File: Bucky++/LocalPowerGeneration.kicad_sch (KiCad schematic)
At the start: 26 parts, among them IC801 TPS629206QDRLRQ1, U2 TPS2116DRLR, U802 LMR36506MSC5RPERQ1

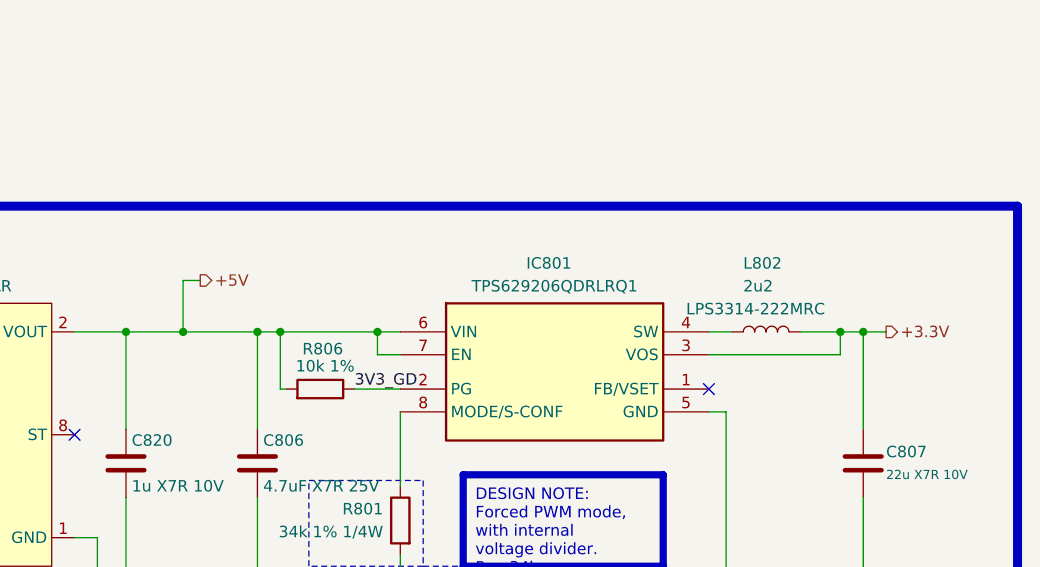
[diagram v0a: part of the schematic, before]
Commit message: added over-current protection on main input
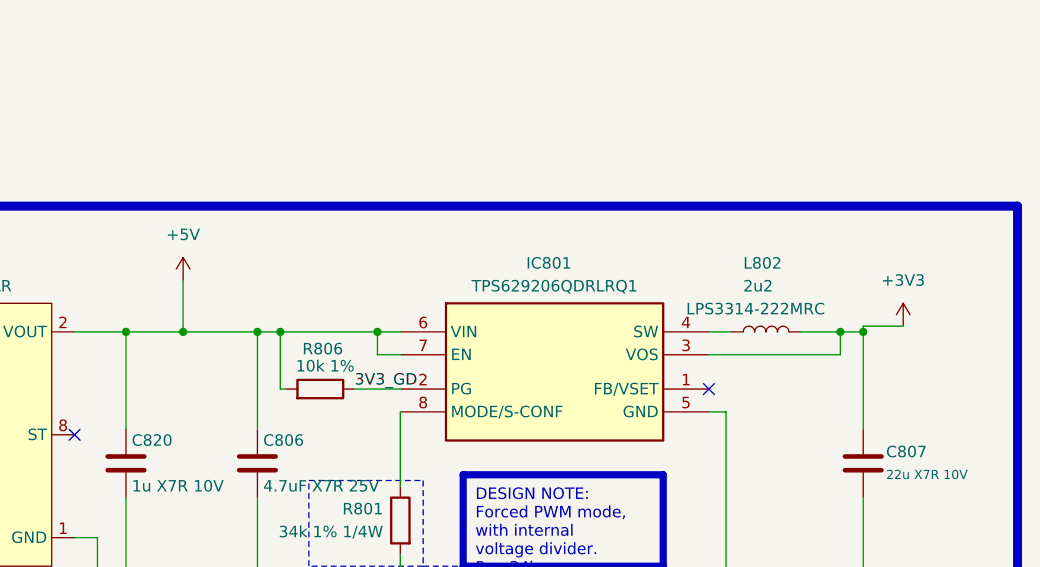
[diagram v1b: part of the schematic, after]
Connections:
- net +3.3V renamed +3V3
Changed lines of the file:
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@@
+	(wire
+		(pts
+			(xy 362.585 77.47) (xy 362.585 78.105)
+		)
+		(stroke
+			(width 0)
+			(type default)
+		)
+	)
 	(wire
 		(pts
@@
 	(wire
 		(pts
-			(xy 288.925 72.39) (xy 287.02 72.39)
-		)
-		(stroke
-			(width 0)
-			(type default)
-		)
-	)
-	(wire
-		(pts
 			(xy 174.625 78.105) (xy 172.085 78.105)
 		)
@@
 	(wire
 		(pts
-			(xy 362.585 78.105) (xy 365.125 78.105)
+			(xy 362.585 77.47) (xy 367.03 77.47)
 		)
 		(stroke
@@
 			)
 			(justify right)
-		)
-	)
-	(hierarchical_label "+3.3V"
-		(shape output)
-		(at 365.125 78.105 0)
-		(effects
-			(font
-				(size 1.27 1.27)
-			)
-			(justify left)
-		)
-	)
-	(hierarchical_label "+5V"
-		(shape output)
-		(at 288.925 72.39 0)
-		(effects
-			(font
-				(size 1.27 1.27)
-			)
-			(justify left)
 		)
 	)
@@
 	)
 	(symbol
+		(lib_id "power:+5V")
+		(at 287.02 72.39 0)
+		(unit 1)
+		(exclude_from_sim no)
+		(in_bom yes)
+		(on_board yes)
+		(dnp no)
+		(fields_autoplaced yes)
+		(property "Reference" "#PWR087"
+			(at 287.02 76.2 0)
+			(effects
+				(font
+					(size 1.27 1.27)
+				)
+				(hide yes)
+			)
+		)
+		(property "Value" "+5V"
+			(at 287.02 67.31 0)
+			(effects
+				(font
+					(size 1.27 1.27)
+				)
+			)
+		)
+		(property "Footprint" ""
+			(at 287.02 72.39 0)
+			(effects
+				(font
+					(size 1.27 1.27)
+				)
+				(hide yes)
+			)
+		)
+		(property "Datasheet" ""
+			(at 287.02 72.39 0)
+			(effects
+				(font
+					(size 1.27 1.27)
+				)
+				(hide yes)
+			)
+		)
+		(property "Description" "Power symbol creates a global label with name \"+5V\""
+			(at 287.02 72.39 0)
+			(effects
+				(font
+					(size 1.27 1.27)
+				)
+				(hide yes)
+			)
+		)
+		(pin "1"
+		)
+		(instances
+			(project ""
+				(path "/0650c7a8-acba-429c-9f8e-eec0baf0bc1c/fede4c36-00cc-4d3d-b71c-5243ba232202/20f2e49e-3c3c-4877-a054-2792c8a24538"
+					(reference "#PWR087")
+					(unit 1)
+				)
+			)
+		)
+	)
+	(symbol
 		(lib_id "Device:R")
 		(at 238.125 82.55 0)
@@
 					(unit 1)
 				)
+			)
+		)
+	)
+	(symbol
+		(lib_id "power:+3V3")
+		(at 367.03 77.47 0)
+		(unit 1)
+		(exclude_from_sim no)
+		(in_bom yes)
+		(on_board yes)
+		(dnp no)
+		(fields_autoplaced yes)
+		(property "Reference" "#PWR086"
+			(at 367.03 81.28 0)
+			(effects
+				(font
+					(size 1.27 1.27)
+				)
+				(hide yes)
+			)
+		)
+		(property "Value" "+3V3"
+			(at 367.03 72.39 0)
+			(effects
+				(font
+					(size 1.27 1.27)
+				)
+			)
+		)
+		(property "Footprint" ""
+			(at 367.03 77.47 0)
+			(effects
+				(font
+					(size 1.27 1.27)
+				)
+				(hide yes)
+			)
+		)
+		(property "Datasheet" ""
+			(at 367.03 77.47 0)
+			(effects
+				(font
+					(size 1.27 1.27)
+				)
+				(hide yes)
+			)
+		)
+		(property "Description" "Power symbol creates a global label with name \"+3V3\""
+			(at 367.03 77.47 0)
+			(effects
+				(font
+					(size 1.27 1.27)
+				)
+				(hide yes)
+			)
+		)
+		(pin "1"
+		)
+		(instances
+			(project ""
+				(path "/0650c7a8-acba-429c-9f8e-eec0baf0bc1c/fede4c36-00cc-4d3d-b71c-5243ba232202/20f2e49e-3c3c-4877-a054-2792c8a24538"
+					(reference "#PWR086")
+					(unit 1)
+				)

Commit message: more routing
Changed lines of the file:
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@@
 		(exclude_from_sim no)
 		(at 318.135 93.98 0)
-		(size 22.225 10.16)
+		(size 22.225 12.7)
 		(margins 1.3525 1.3525 1.3525 1.3525)
 		(stroke
